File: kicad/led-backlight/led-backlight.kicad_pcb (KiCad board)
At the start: 2 copper layers, 62.5 x 52.6 mm, 18 parts, among them J1 Conn_01x03, Q1 BSS138, SW1 SW_MEC_5E, U1 AMS1117-3.3, U2 SeeeduinoXIAO, U3 AMS1117-3.3

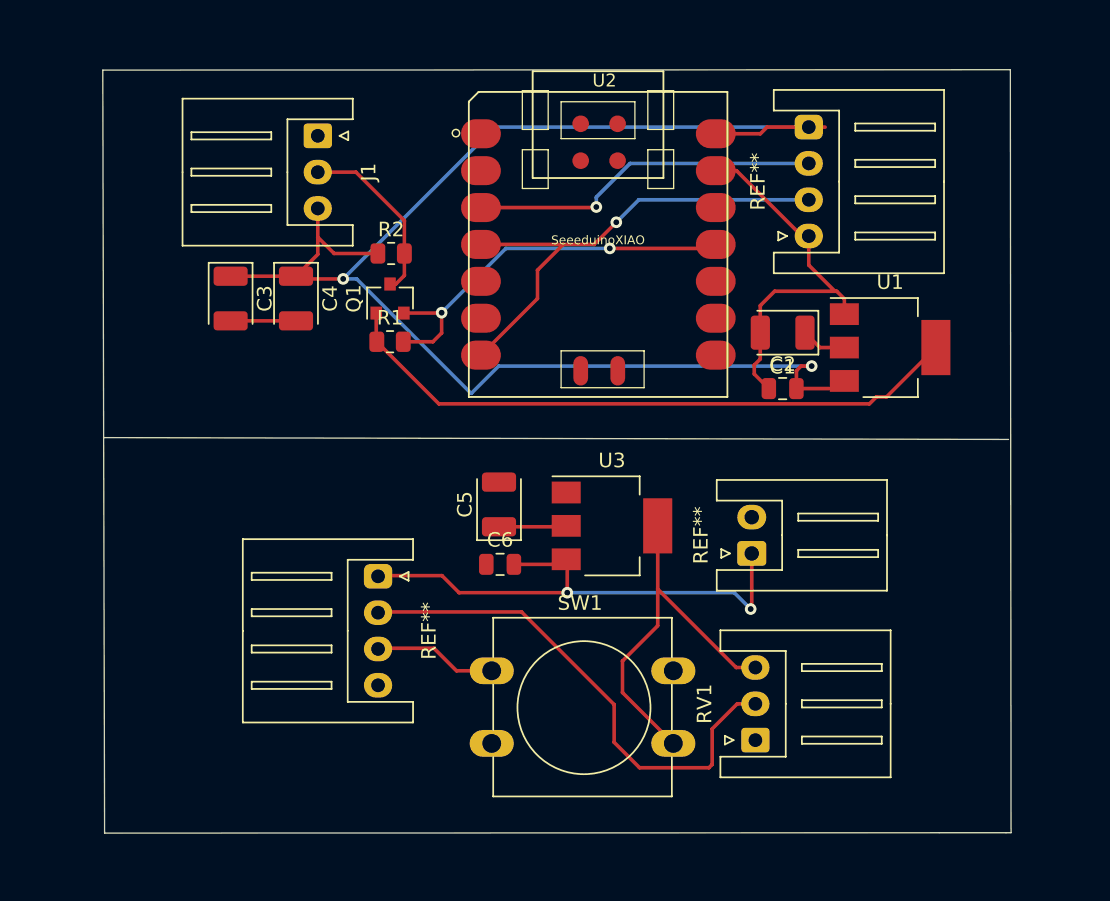
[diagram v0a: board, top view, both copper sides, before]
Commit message: update board track routing
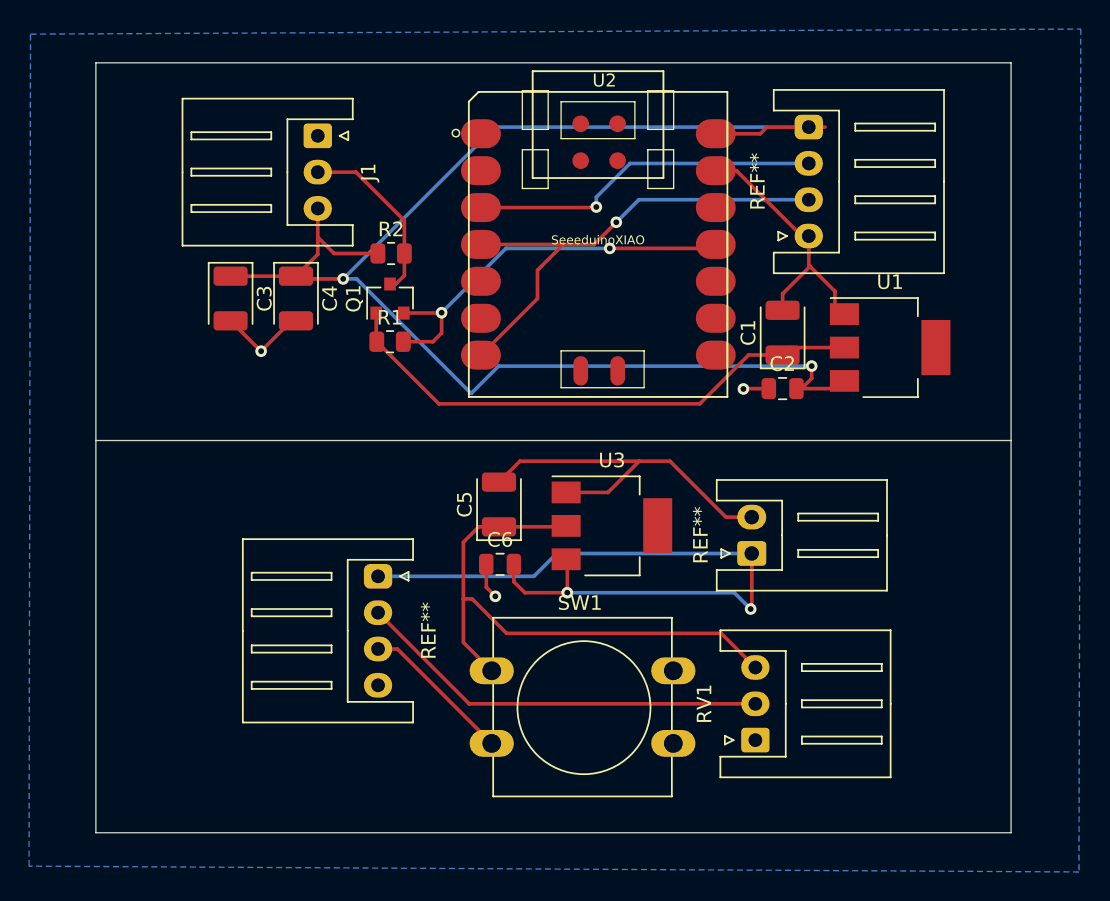
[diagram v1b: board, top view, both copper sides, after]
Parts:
- turned C1 to 90 degrees
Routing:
- net GND: track 31.1 -> 54.4 mm, vias 0 -> 3
- net +5V: track 139.8 -> 155.2 mm
- net /mcu_board/mode_btn: track 72.4 -> 83.6 mm
- net /mcu_board/+3V: track 47.0 -> 37.6 mm
- net /mcu_board/mode_ref: track 58.5 -> 52.8 mm
- added copper zone on B.Cu, net GND
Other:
- board size 62.5 x 52.6 mm -> 63 x 53 mm

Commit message: finish kicad project v1
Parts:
- renumbered REF** to J2, REF** to J3, REF** to J4
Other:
- outline, holes or cut-outs redrawn

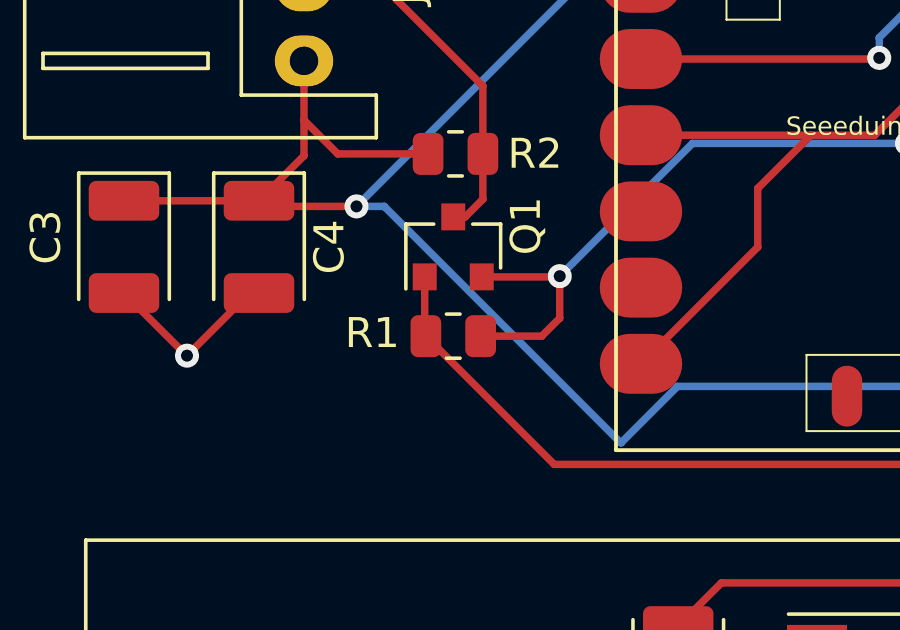
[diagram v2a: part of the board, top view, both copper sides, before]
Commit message: add pulldown resistor to eic pin
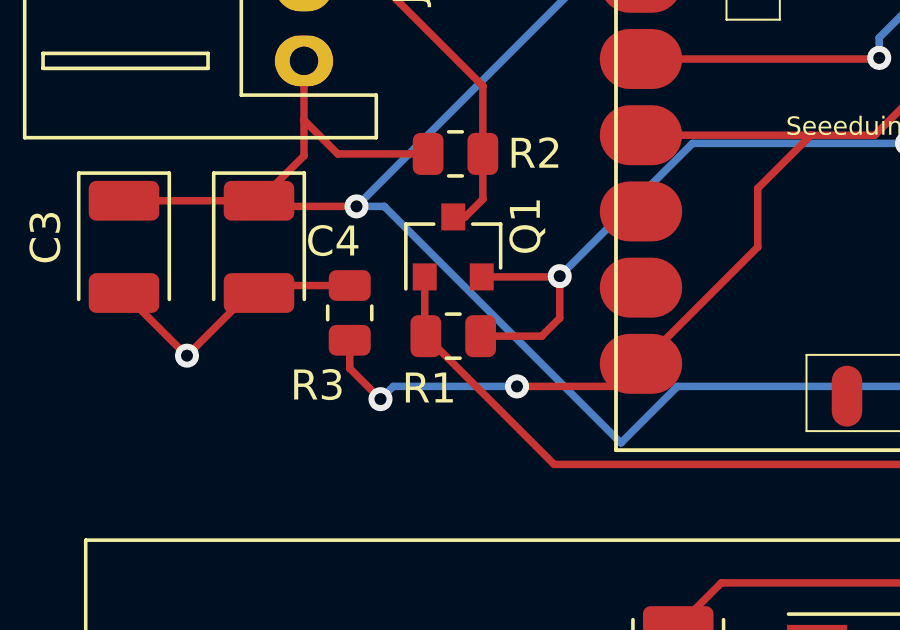
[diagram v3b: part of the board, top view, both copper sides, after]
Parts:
- added R3: R_0805_2012Metric, Resistor_SMD:R_0805_2012Metric, F.Cu at (173.8, 110.4)
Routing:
- net /mcu_board/mode_btn: track 83.6 -> 95.1 mm, vias 1 -> 3
- net GND: track 54.4 -> 57.5 mm
